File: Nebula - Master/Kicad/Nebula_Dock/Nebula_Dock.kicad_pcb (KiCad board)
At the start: 2 copper layers, 40 x 40 mm, 22 parts, among them J1 Male_watch_connector, J2 USB_C_Receptacle_USB2.0, U1 FT232RL

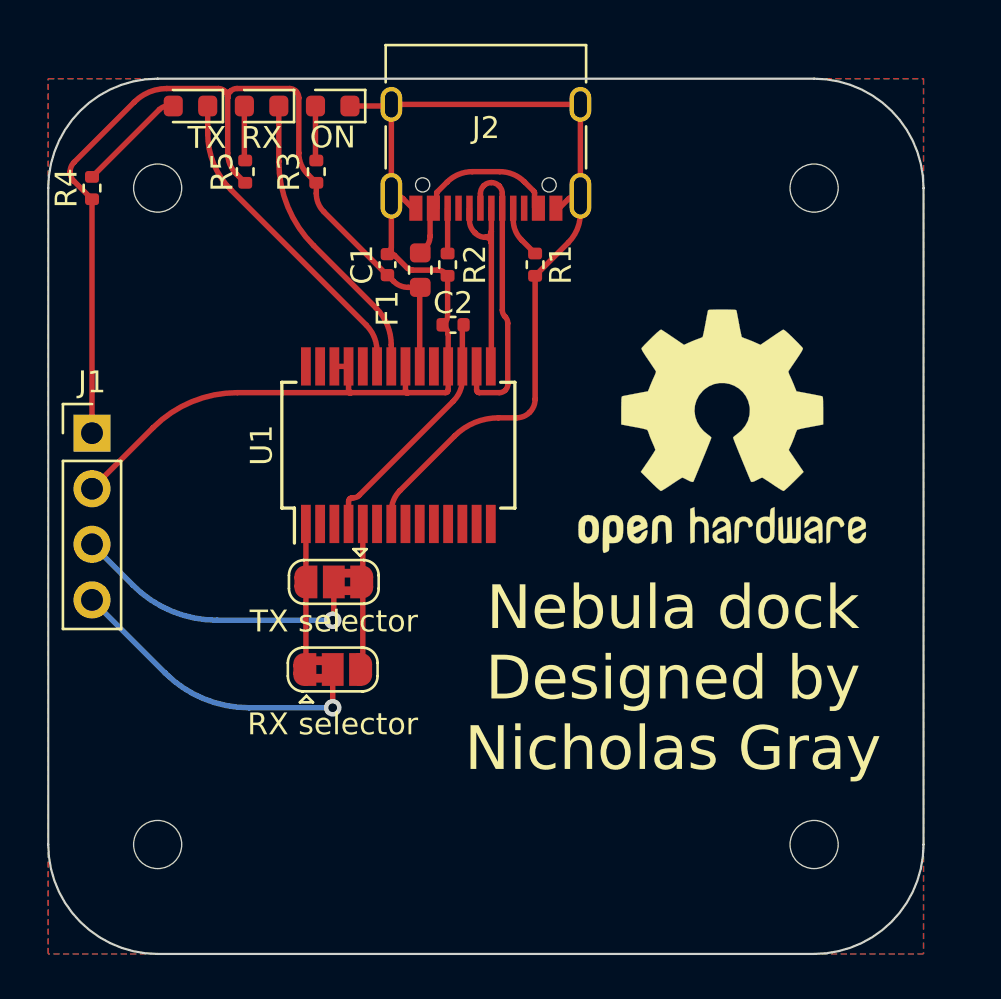
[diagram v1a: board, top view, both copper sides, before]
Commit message: changed prgm pin on dock
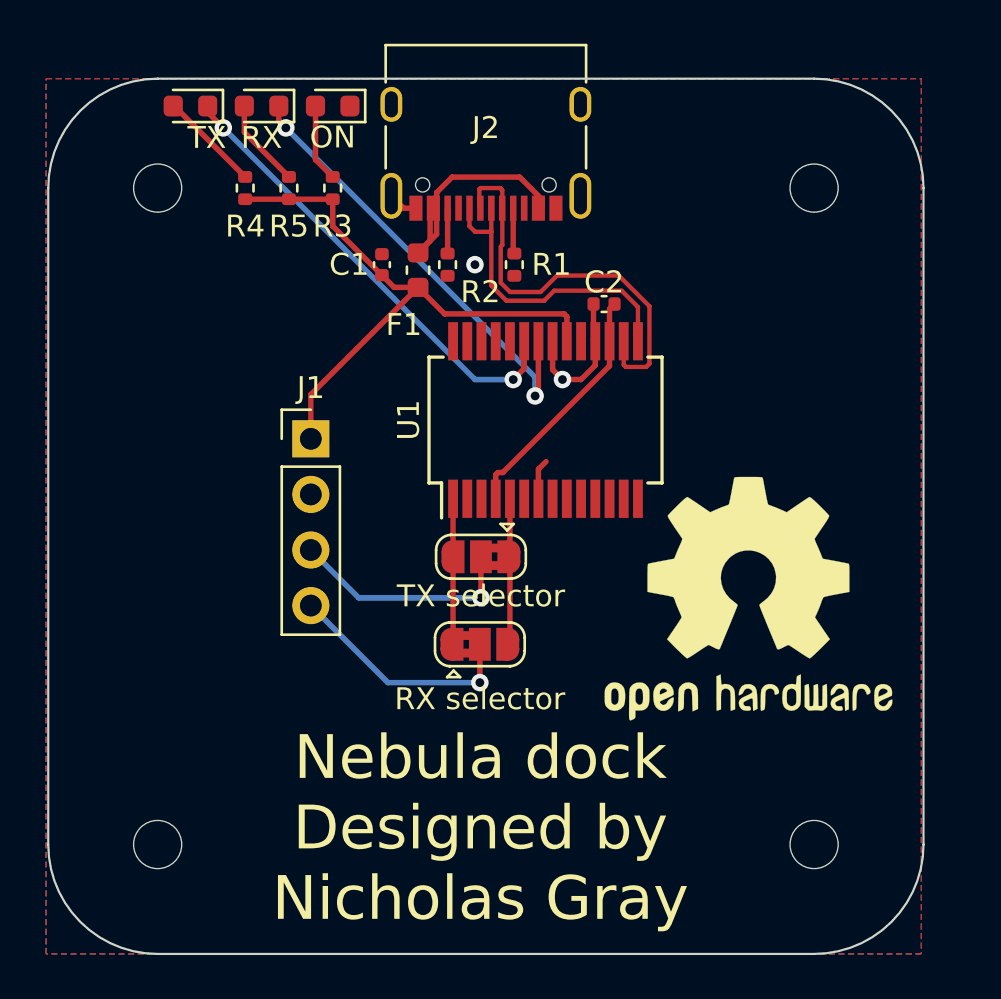
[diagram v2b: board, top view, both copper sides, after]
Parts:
- moved J1 10.0 mm to (172.0, 71.5)
- moved REF** 7.74 mm to (192.0, 78.8)
- moved R4 7.00 mm to (169.0, 60.0)
- moved C2 6.97 mm to (185.4, 65.3)
- moved RX selector 6.82 mm to (179.7, 80.8)
- moved TX selector 6.82 mm to (179.8, 76.8)
- moved U1 6.82 mm to (182.7, 70.6)
- moved R5 2.14 mm to (171.0, 60.0)
- moved R3 1.06 mm to (173.0, 60.0)
- moved R1 0.95 mm to (181.3, 63.5)
- moved C1 0.25 mm to (175.2, 63.5)
- moved F1 0.10 mm to (176.9, 63.8)
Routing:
- net GND: track 73.8 -> 9.59 mm, vias 0 -> 2
- net V_USB: track 44.5 -> 27.7 mm
- net Net-(D3-Pad1): track 13.9 -> 20.7 mm, vias 0 -> 2
- net Net-(D2-Pad1): track 15.1 -> 21.3 mm, vias 0 -> 2
- net USB-: track 13.8 -> 19.1 mm
- net USB+: track 9.79 -> 14.5 mm
- net ESP_RX: track 14.5 -> 10.9 mm
- net ESP_TX: track 13.9 -> 10.6 mm
- net Net-(J2-PadA4): track 8.75 -> 11.3 mm
- net Net-(D3-Pad2): track 2.75 -> 4.08 mm
- net Net-(D1-Pad2): track 2.75 -> 3.57 mm

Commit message: 3d files
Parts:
- moved J1 4.99 mm to (172.0, 76.5)
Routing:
- net V_USB: track 27.7 -> 32.4 mm
- net GND: track 9.59 -> 12.3 mm
- net Net-(J2-PadA4): track 11.3 -> 10.2 mm
- net ESP_RX: track 10.9 -> 9.96 mm
- net USB+: track 14.5 -> 15.1 mm
